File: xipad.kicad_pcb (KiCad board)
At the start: 2 copper layers, 179 x 90 mm, 43 parts, among them SW1 SW_Push, SW10 SW_Push, SW11 SW_Push, SW12 SW_Push, SW13 SW_Push, SW14 SW_Push, SW15 SW_Push, SW16 SW_Push, SW17 SW_Push, SW18 SW_Push, SW19 SW_Push, SW2 SW_Push, SW3 SW_Push, SW4 SW_Push, SW5 SW_Push, SW6 SW_Push, SW7 SW_Push, SW8 SW_Push, SW9 SW_Push, U1 ProMicro

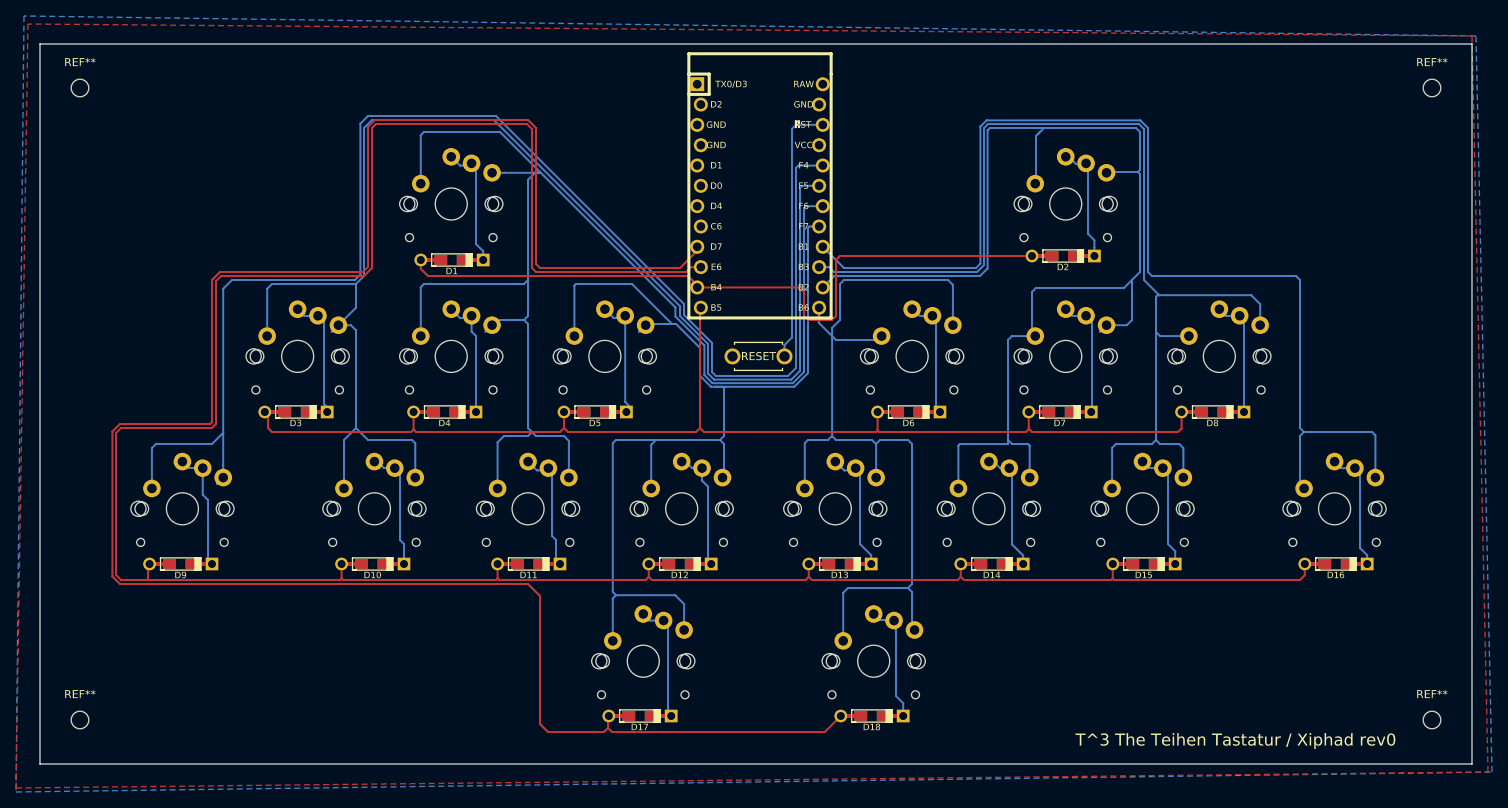
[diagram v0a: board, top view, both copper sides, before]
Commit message: revision 1 (remove frontside silk, add center mounting hole.)
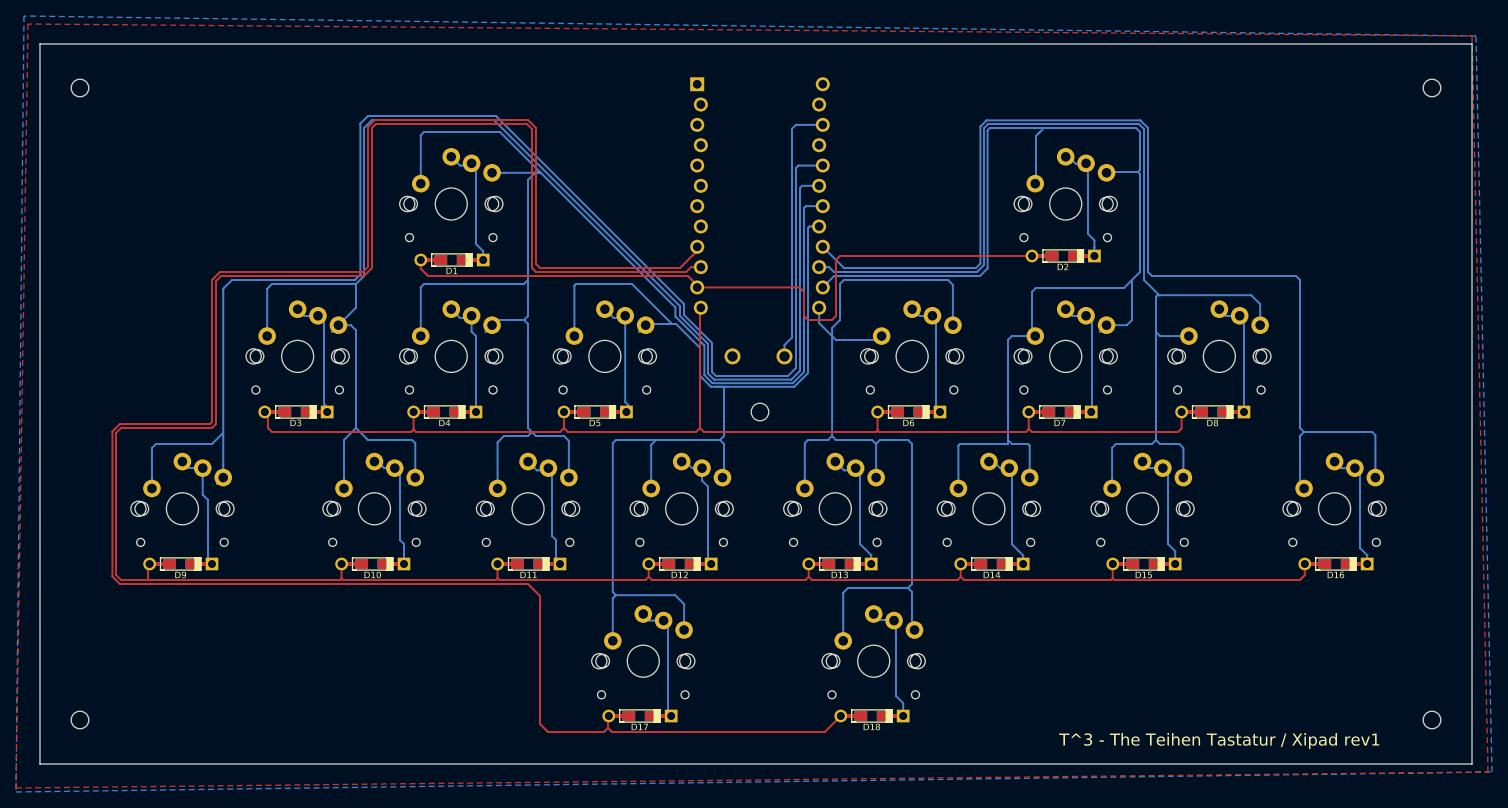
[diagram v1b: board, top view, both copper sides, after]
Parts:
- added REF**: MountingHole_2.2mm_M2, MountingHole:MountingHole_2.2mm_M2, F.Cu at (101.0, 26.0)
- U1: footprint Keebio-Parts:ArduinoProMicro-ZigZag -> Keebio-Parts:ArduinoProMicro-ZigZag-CleanFront
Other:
- board text added: "T^3 - The Teihen Tastatur / Xipad rev1"
- board text removed: "T^3 The Teihen Tastatur / Xiphad rev0"
